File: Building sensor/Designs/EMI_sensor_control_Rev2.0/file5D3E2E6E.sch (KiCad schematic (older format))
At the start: 0 parts

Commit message: overdue backup
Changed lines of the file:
@@
 $Descr A4 11693 8268
 encoding utf-8
-Sheet 4 9
+Sheet 4 8
 Title "Pancreas EMI Conductivity Meter "
 Date ""
@@
 $EndSheet
 $Sheet
-S 2500 3550 3050 1950
-U 5D3AC029
-F0 "FPGA" 50
-F1 "file5D3AC028.sch" 50
-$EndSheet
-$Sheet

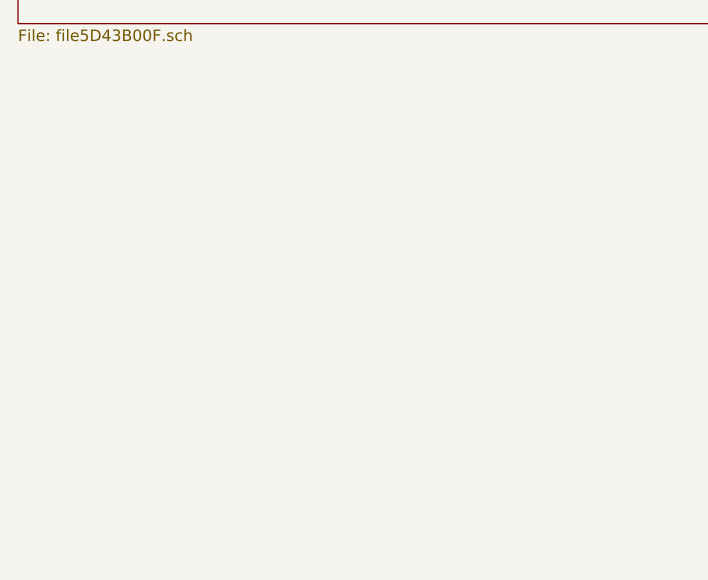
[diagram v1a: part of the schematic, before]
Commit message: Rev 2.0 Complete
Rev 2.0 of PCB Completed
SCHM, PCB layout, and gerber files generated
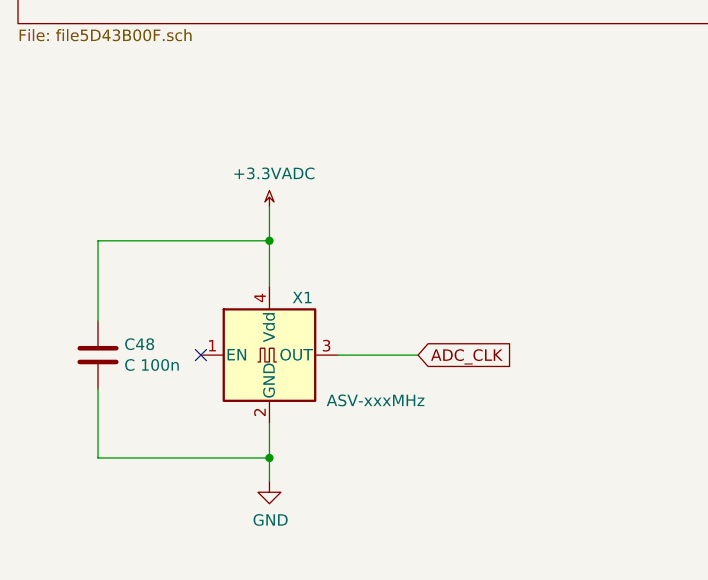
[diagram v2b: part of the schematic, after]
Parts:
- added C48: C 100n, Capacitor_SMD:C_0603_1608Metric_Pad1.05x0.95mm_HandSolder, symbol Device:C
- added X1: ASV-xxxMHz, Oscillator:Oscillator_SMD_Abracon_ASV-4Pin_7.0x5.1mm, symbol Oscillator:ASV-xxxMHz
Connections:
- new net +3.3VADC: C48.1, X1.4 (Vdd)
- new net ADC_CLK: X1.3 (OUT)
- new net GND: C48.2, X1.2 (GND)
- no-connect marks 0 -> 1
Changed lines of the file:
@@
 F1 "file5D43B00F.sch" 50
 $EndSheet
+$Comp
+L Oscillator:ASV-xxxMHz X1
+U 1 1 5E7D7BFA
+P 3600 4700
+F 0 "X1" H 3700 4950 50  0000 L CNN
+F 1 "ASV-xxxMHz" H 3850 4500 50  0000 L CNN
+F 2 "Oscillator:Oscillator_SMD_Abracon_ASV-4Pin_7.0x5.1mm" H 4300 4350 50  0001 C CNN
+F 3 "http://www.abracon.com/Oscillators/ASV.pdf" H 3500 4700 50  0001 C CNN
+	1    3600 4700
+	1    0    0    -1
+$EndComp
+NoConn ~ 3300 4700
+$Comp
+L power:+3.3VADC #PWR072
+U 1 1 5E7D80ED
+P 3600 4050
+F 0 "#PWR072" H 3750 4000 50  0001 C CNN
+F 1 "+3.3VADC" H 3620 4193 50  0000 C CNN
+F 2 "" H 3600 4050 50  0001 C CNN
+F 3 "" H 3600 4050 50  0001 C CNN
+	1    3600 4050
+	1    0    0    -1
+$EndComp
+$Comp
+L power:GND #PWR073
+U 1 1 5E7D8489
+P 3600 5250
+F 0 "#PWR073" H 3600 5000 50  0001 C CNN
+F 1 "GND" H 3605 5077 50  0000 C CNN
+F 2 "" H 3600 5250 50  0001 C CNN
+F 3 "" H 3600 5250 50  0001 C CNN
+	1    3600 5250
+	1    0    0    -1
+$EndComp
+$Comp
+L Device:C C48
+U 1 1 5E7D896F
+P 2850 4700
+F 0 "C48" H 2965 4746 50  0000 L CNN
+F 1 "C 100n" H 2965 4655 50  0000 L CNN
+F 2 "Capacitor_SMD:C_0603_1608Metric_Pad1.05x0.95mm_HandSolder" H 2888 4550 50  0001 C CNN
+F 3 "~" H 2850 4700 50  0001 C CNN
+	1    2850 4700
+	1    0    0    -1
+$EndComp
+Wire Wire Line
+	2850 4850 2850 5150
+Wire Wire Line
+	2850 5150 3600 5150
+Wire Wire Line
+	3600 5150 3600 5000
+Wire Wire Line
+	3600 5150 3600 5250
+Connection ~ 3600 5150
+Wire Wire Line
+	2850 4550 2850 4200
+Wire Wire Line
+	2850 4200 3600 4200
+Wire Wire Line
+	3600 4200 3600 4400
+Wire Wire Line
+	3600 4200 3600 4050
+Connection ~ 3600 4200
+Text GLabel 4250 4700 2    50   Input ~ 0
+ADC_CLK
+Wire Wire Line
+	4250 4700 3900 4700
 $EndSCHEMATC
